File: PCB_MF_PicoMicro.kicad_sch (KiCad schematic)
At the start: 10 parts, among them J1 Conn_01x12, J2 Conn_01x12, J7 Conn_01x02_Pin, J8 Conn_01x02_Pin

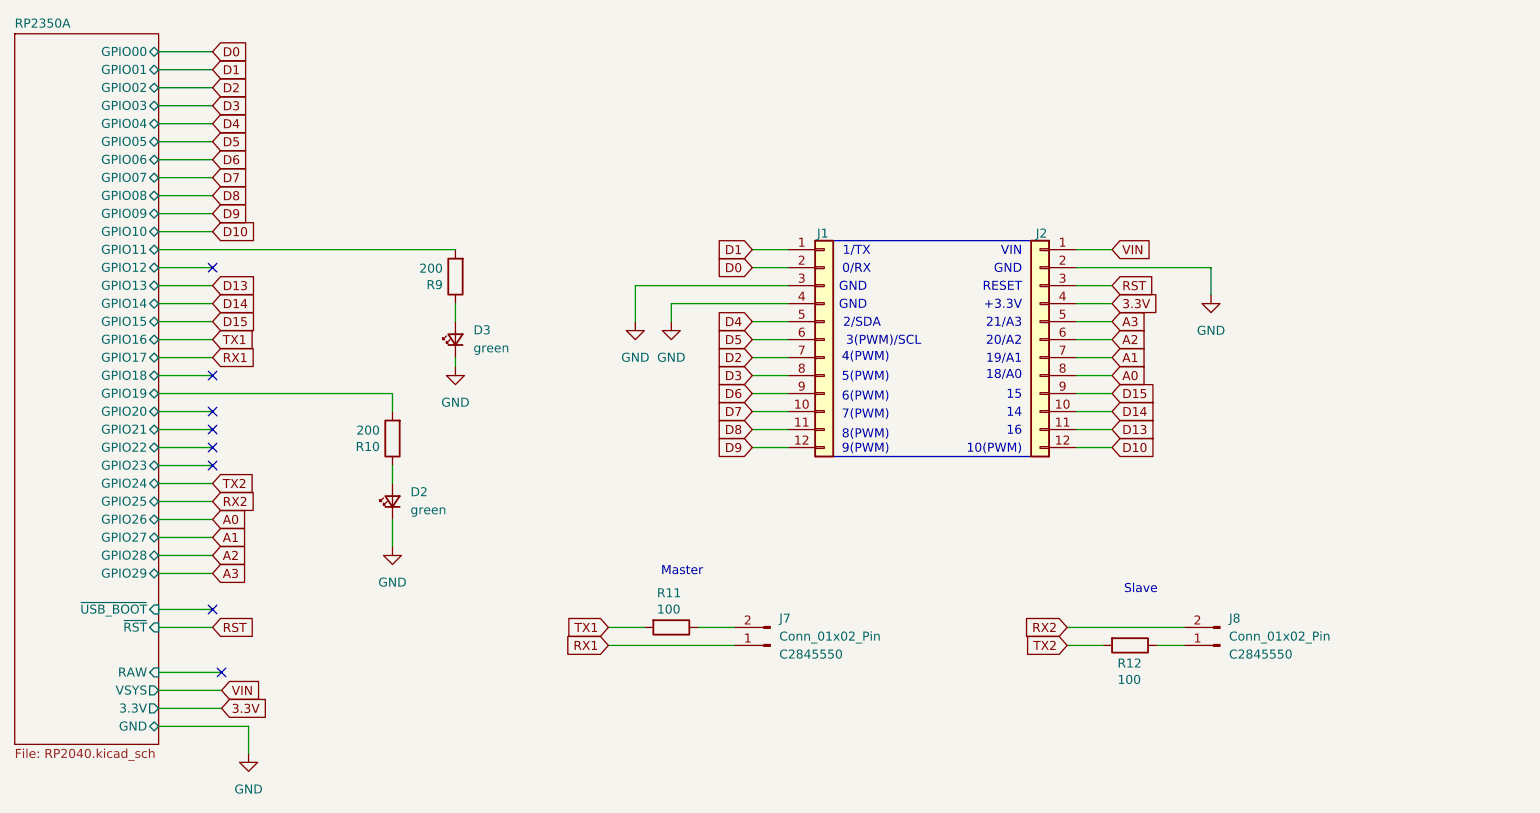
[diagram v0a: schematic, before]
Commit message: route both additional resistors
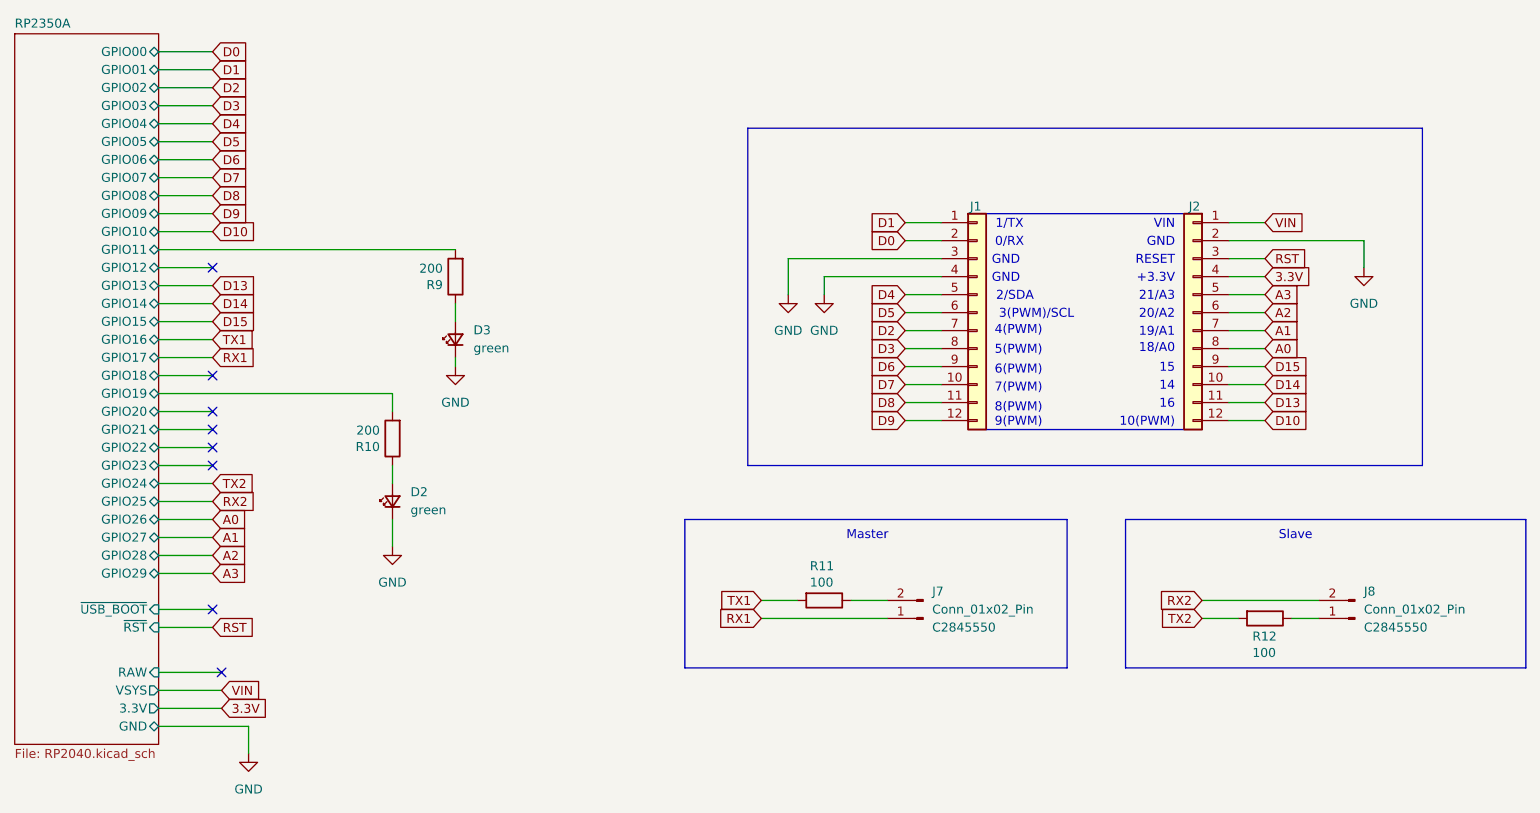
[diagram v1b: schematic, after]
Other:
- moved on the sheet: J1, J2, J7, J8, R11, R12

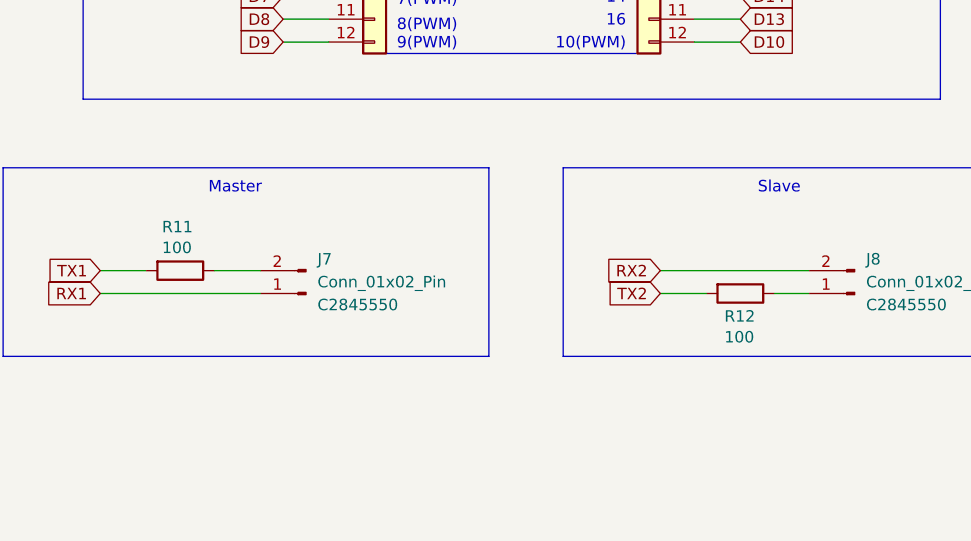
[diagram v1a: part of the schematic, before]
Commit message: Swap TX/RX line from connection to slave
* swap tx line to slave, better arrangement of parts
* better positioning of parts
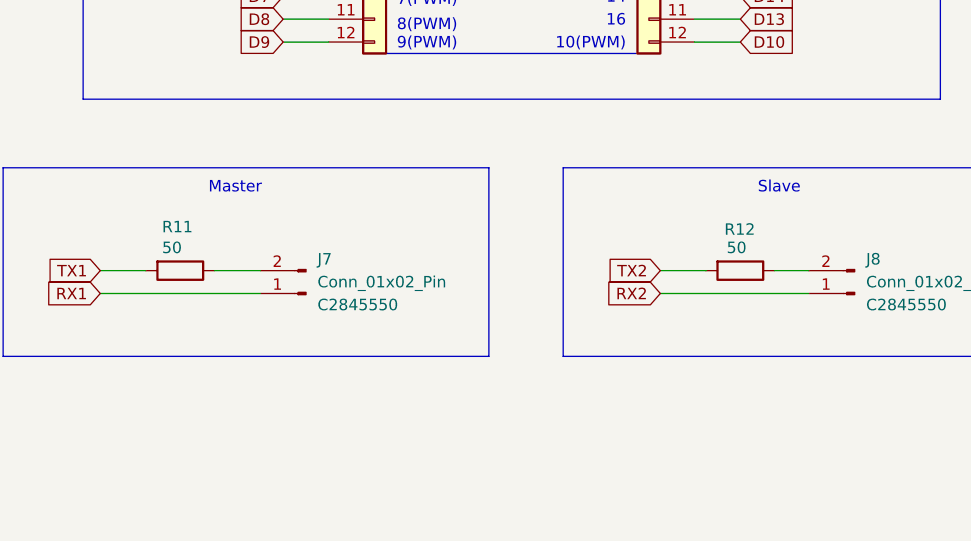
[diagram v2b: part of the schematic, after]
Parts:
- R11, R12: value 100 -> 50
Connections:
- net RX2: now also J8.1 (Pin_1); no longer J8.2 (Pin_2)
- net at R12.1: now also J8.2 (Pin_2); no longer J8.1 (Pin_1)
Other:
- moved on the sheet: R12

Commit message: update production files
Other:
- note added: "PicoMicro"
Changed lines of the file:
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@@
 	)
 	(rectangle
-		(start 162.56 59.69)
-		(end 195.58 90.17)
+		(start 162.56 57.15)
+		(end 195.58 92.71)
 		(stroke
 			(width 0)
@@
 	(rectangle
 		(start 131.445 47.625)
-		(end 226.695 95.25)
+		(end 226.695 97.79)
 		(stroke
 			(width 0)
@@
 		(effects
 			(font
+				(size 1.27 1.27)
+			)
+		)
+	)
+	(text "PicoMicro"
+		(exclude_from_sim no)
+		(at 176.276 51.308 0)
+		(effects
+			(font

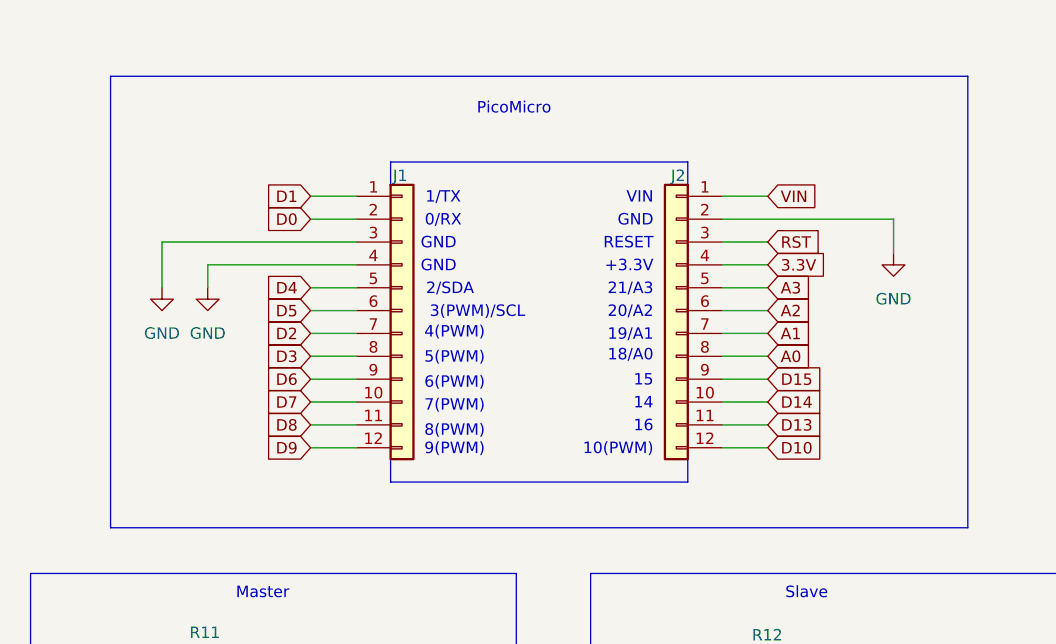
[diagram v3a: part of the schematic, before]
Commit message: use new PicoMicro Symbol and footprint
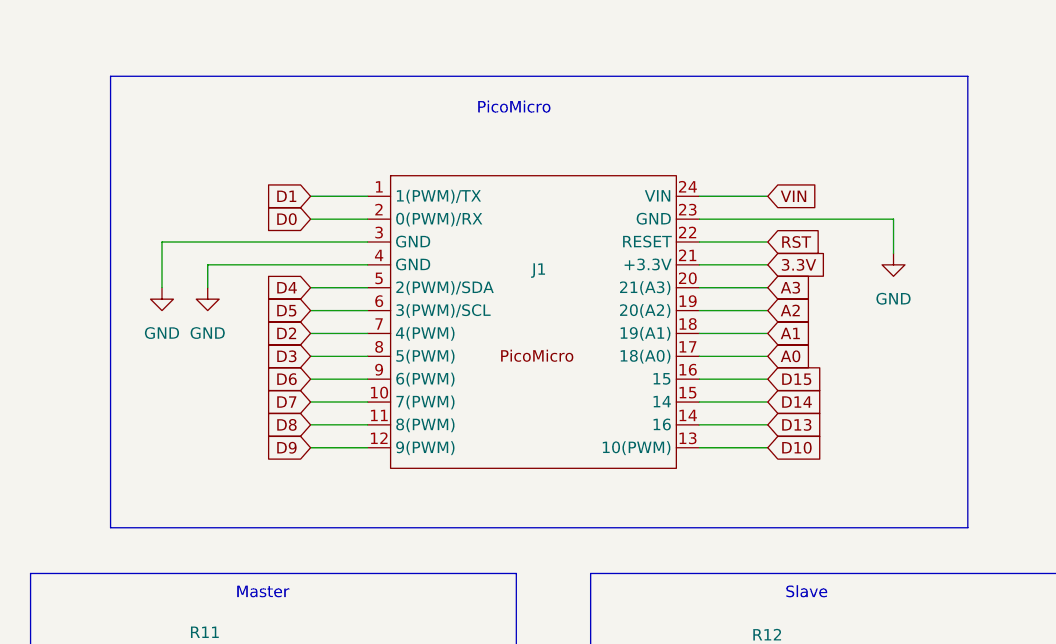
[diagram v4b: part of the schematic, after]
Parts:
- removed J1, J2: Conn_01x12, Connector_PinHeader_2.54mm:PinHeader_1x12_P2.54mm_Vertical, symbol Connector_Generic:Conn_01x12
- added J1: ~, _Own_Library:PicoMicro, symbol Own_Library:PicoMicro
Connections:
- net 3.3V: now also J1.21 (+3.3V)
- net A0: now also J1.17 (18(A0))
- net A1: now also J1.18 (19(A1))
- net A2: now also J1.19 (20(A2))
- net A3: now also J1.20 (21(A3))
- net D0: now also J1.2 (0(PWM)/RX)
- net D1: now also J1.1 (1(PWM)/TX)
- net D10: now also J1.13 (10(PWM))
- net D13: now also J1.14 (16)
- net D14: now also J1.15 (14)
- net D15: now also J1.16 (15)
- net D2: now also J1.7 (4(PWM))
- net D3: now also J1.8 (5(PWM))
- net D4: now also J1.5 (2(PWM)/SDA)
- net D5: now also J1.6 (3(PWM)/SCL)
- net D6: now also J1.9 (6(PWM))
- net D7: now also J1.10 (7(PWM))
- net D8: now also J1.11 (8(PWM))
- net D9: now also J1.12 (9(PWM))
- net GND: now also J1.23 (GND), J1.3 (GND), J1.4 (GND)
- net RST: now also J1.22 (RESET)
- net VIN: now also J1.24 (VIN)
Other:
- note removed: "+3.3V"
- note removed: "0/RX"
- note removed: "1/TX"
- note removed: "10(PWM)"
- note removed: "14"
- note removed: "15"
- note removed: "16"
- note removed: "18/A0"
- note removed: "19/A1"
- note removed: "2/SDA"
- note removed: "20/A2"
- note removed: "21/A3"
- note removed: "3(PWM)/SCL"
- note removed: "4(PWM)"
- note removed: "5(PWM)"
- note removed: "6(PWM)"
- note removed: "7(PWM)"
- note removed: "8(PWM)"
- note removed: "9(PWM)"
- note removed: "GND"
- note removed: "RESET"
- note removed: "VIN"
